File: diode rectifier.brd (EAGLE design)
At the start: 25.4 x 35.6 mm, 15 parts, among them IC1 LM74670, IC11 LM74670, IC2 LM74670, IC3 LM74670, IC4 SQJ960EP N-FET, IC5 SQJ960EP N-FET

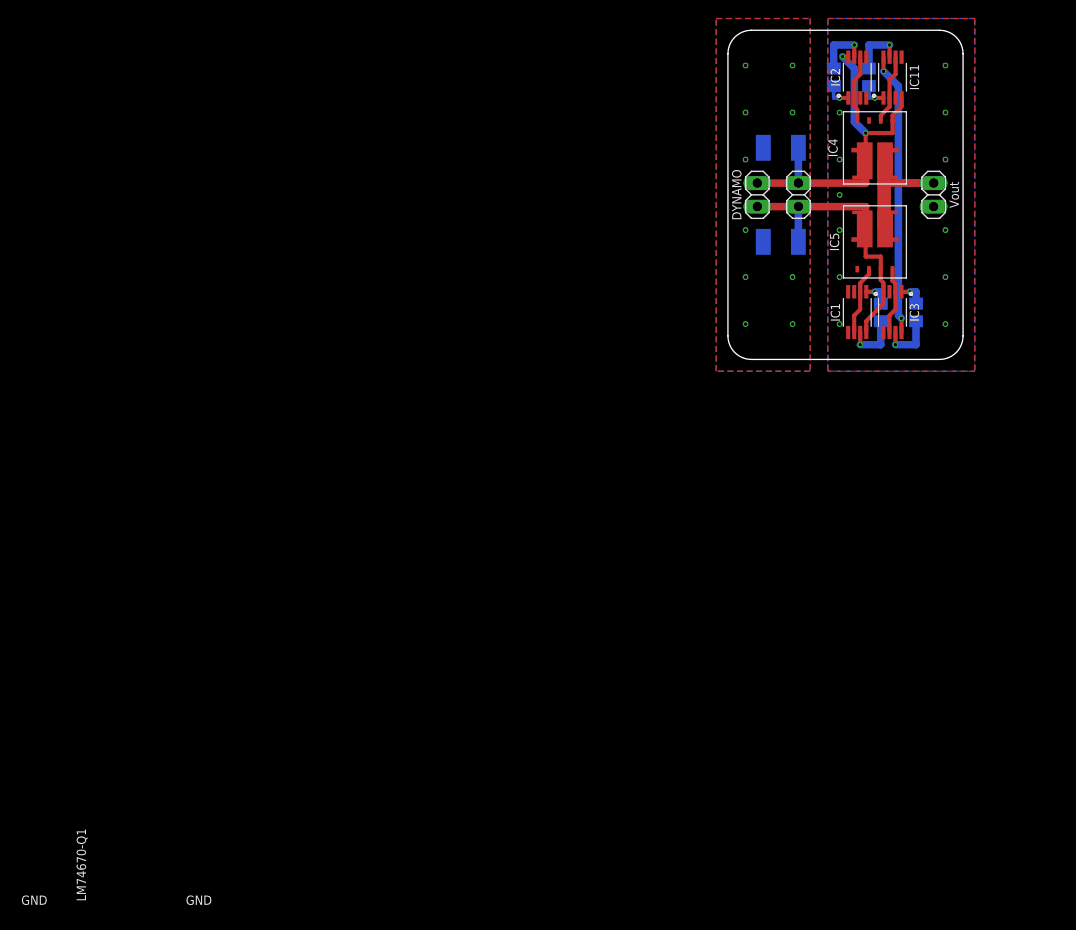
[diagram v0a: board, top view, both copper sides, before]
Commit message: - corrected diode rectifier board layout & regenerated gerbers
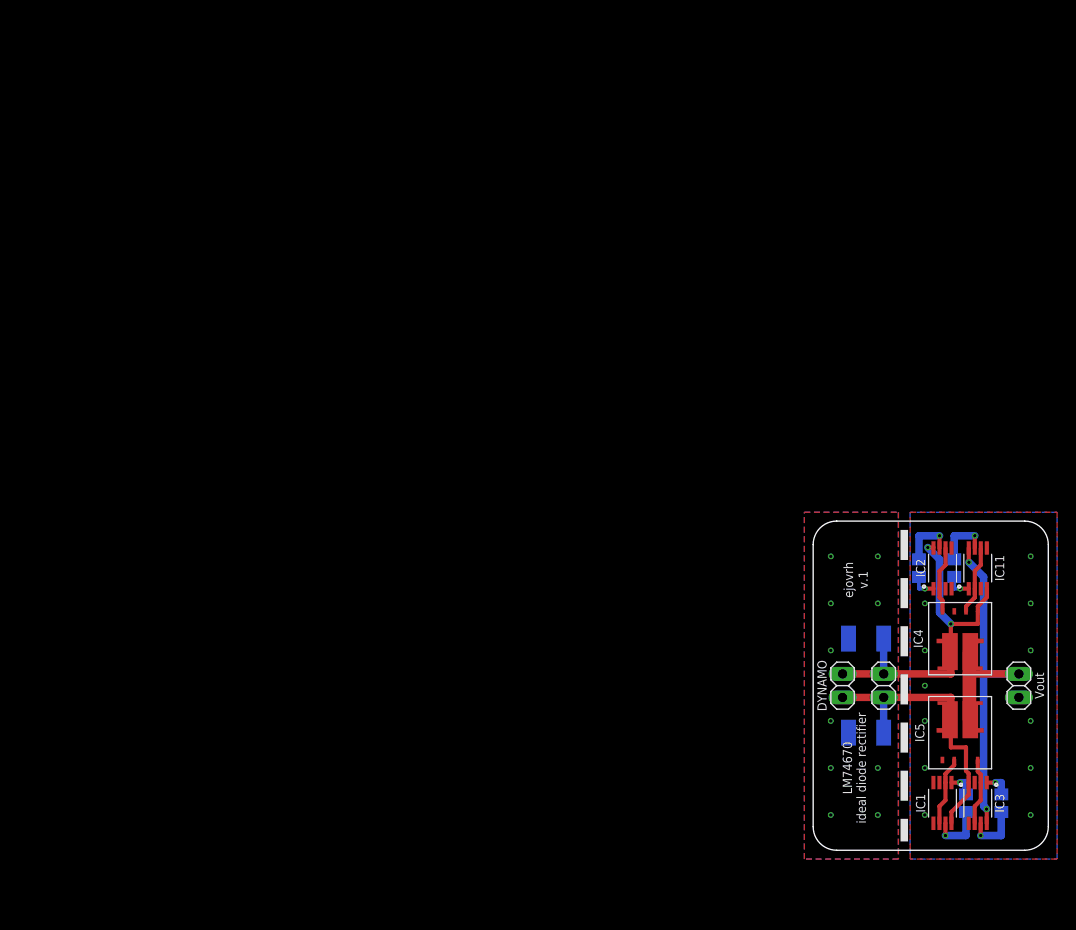
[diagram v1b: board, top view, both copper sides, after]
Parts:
- moved C1 53.8 mm to (18.7, 7.94)
- moved C2 53.8 mm to (22.5, 7.94)
- moved C3 53.8 mm to (17.5, 33.3)
- moved C4 53.8 mm to (13.7, 33.3)
- moved D2 53.8 mm to (7.94, 15.6)
- moved IC1 53.8 mm to (16.2, 7.94)
- moved IC11 53.8 mm to (20.0, 33.3)
- moved IC2 53.8 mm to (16.2, 33.3)
- moved IC3 53.8 mm to (20.0, 7.94)
- moved IC5 53.8 mm to (18.1, 15.6)
- moved D1 53.8 mm to (7.94, 25.7)
- moved DYN1 53.8 mm to (5.40, 20.6)
- moved DYN2 53.8 mm to (9.84, 20.6)
- moved IC4 53.8 mm to (18.1, 25.7)
- moved VOUT 53.8 mm to (24.4, 20.6)
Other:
- board text added: "LM74670 ideal diode rectifier"
- board text removed: "GND"
- board text removed: "LM74670-Q1"
